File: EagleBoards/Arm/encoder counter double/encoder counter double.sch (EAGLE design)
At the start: 15 parts, among them X2 22-23-2021_100MILHEADER, X3 22-23-2041, X4 22-23-2021_100MILHEADER, X5 22-23-2021_100MILHEADER, X6 22-23-2021_100MILHEADER

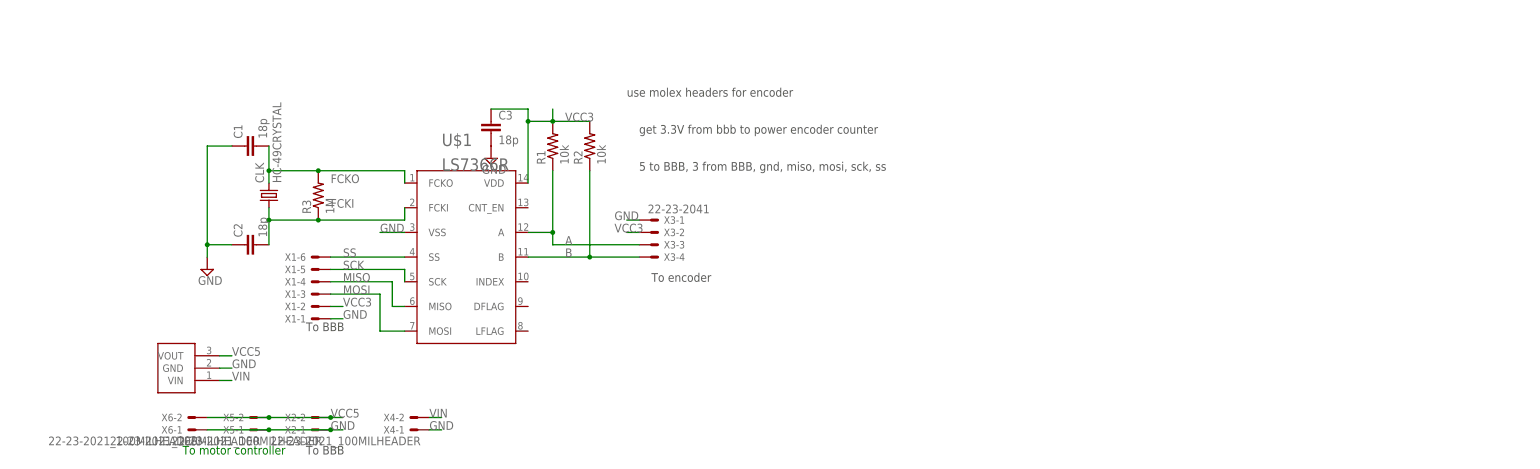
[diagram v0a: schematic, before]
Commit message: pre silk encoder brds. layout ready for review
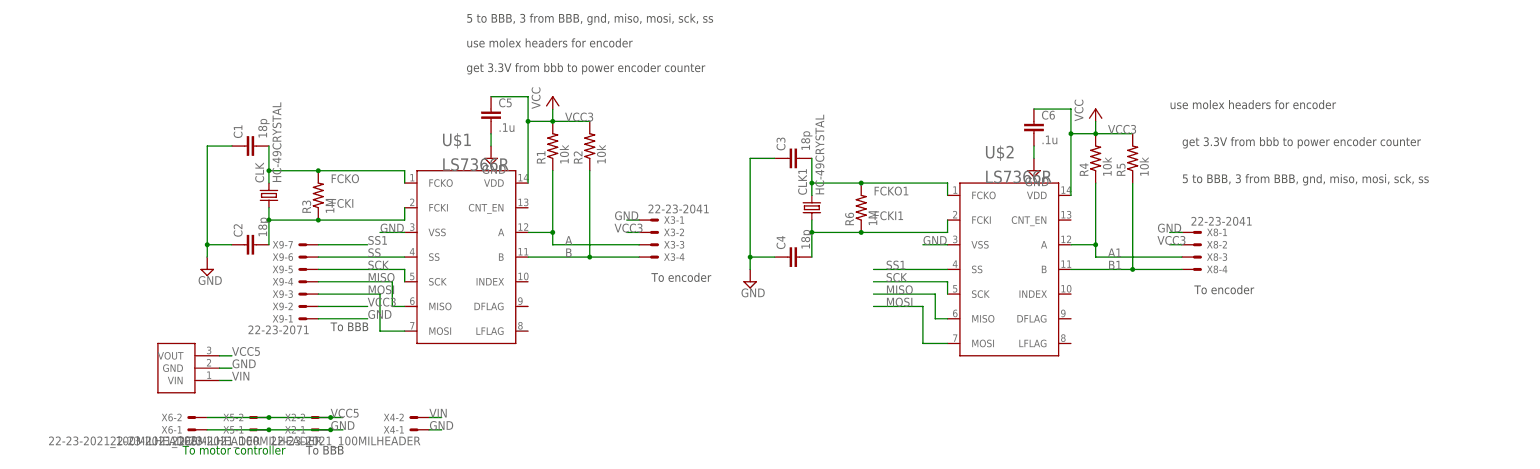
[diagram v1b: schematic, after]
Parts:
- removed X1: (no value), HuskyRobotics17-18:22-23-2061
- added C4: 18p, rcl:C-EUC1206
- added C5, C6: .1u, rcl:C-EUC1206
- added CLK1: HC-49CRYSTAL, HuskyRobotics17-18:HC-49CRYSTAL
- added R4, R5: 10k, rcl:R-US_R1206
- added R6: 1M, rcl:R-US_R1206
- added U$2: LS7366R, HuskyRobotics17-18:LS7366R
- added X8: 22-23-2041, HuskyRobotics17-18:22-23-2041
- added X9: 22-23-2071, con-molex:22-23-2071
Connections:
- new net A1: R4.1, U$2.A, X8-3.S
- new net B1: R5.1, U$2.B, X8-4.S
- new net FCKI1: C4.2, CLK1.1, R6.1, U$2.FCKI
- new net FCKO1: C3.2, CLK1.2, R6.2, U$2.FCKO
- new net SS1: U$2.SS, X9-7.S
- net GND: now also C3.1, C4.1, C5.2, C6.2, U$2.VSS, X8-1.S, X9-1.S; no longer C3.2, X1-1.S
- net MISO: now also U$2.MISO, X9-4.S; no longer X1-4.S
- net MOSI: now also U$2.MOSI, X9-3.S; no longer X1-3.S
- net SCK: now also U$2.SCK, X9-5.S; no longer X1-5.S
- net SS: now also X9-6.S; no longer X1-6.S
- net VCC3: now also C5.1, C6.1, R4.2, R5.2, U$2.VDD, X8-2.S, X9-2.S; no longer C3.1, X1-2.S
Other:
- moved on the sheet: C3
